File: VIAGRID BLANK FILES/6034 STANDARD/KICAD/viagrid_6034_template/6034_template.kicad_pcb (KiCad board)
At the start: 2 copper layers, 60 x 34 mm, 0 parts

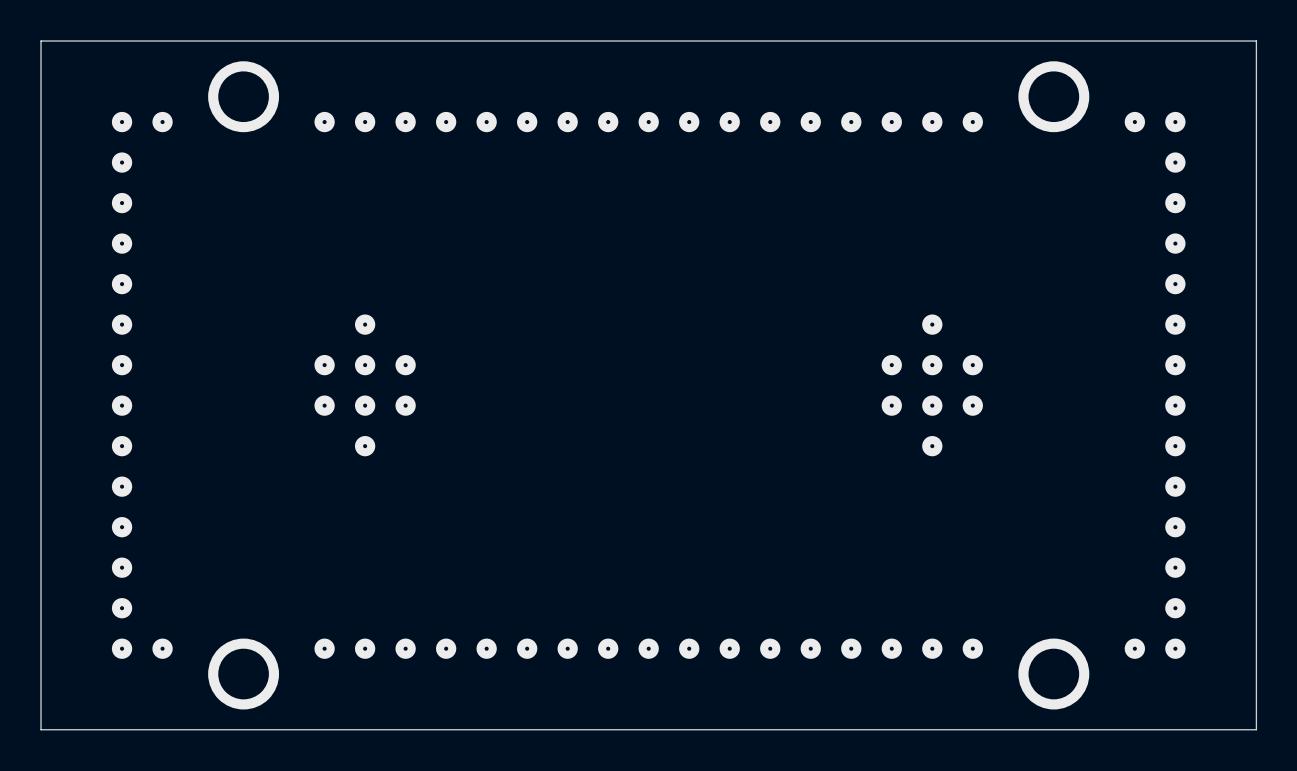
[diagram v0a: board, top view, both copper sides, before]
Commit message: added copper fill and soldermask
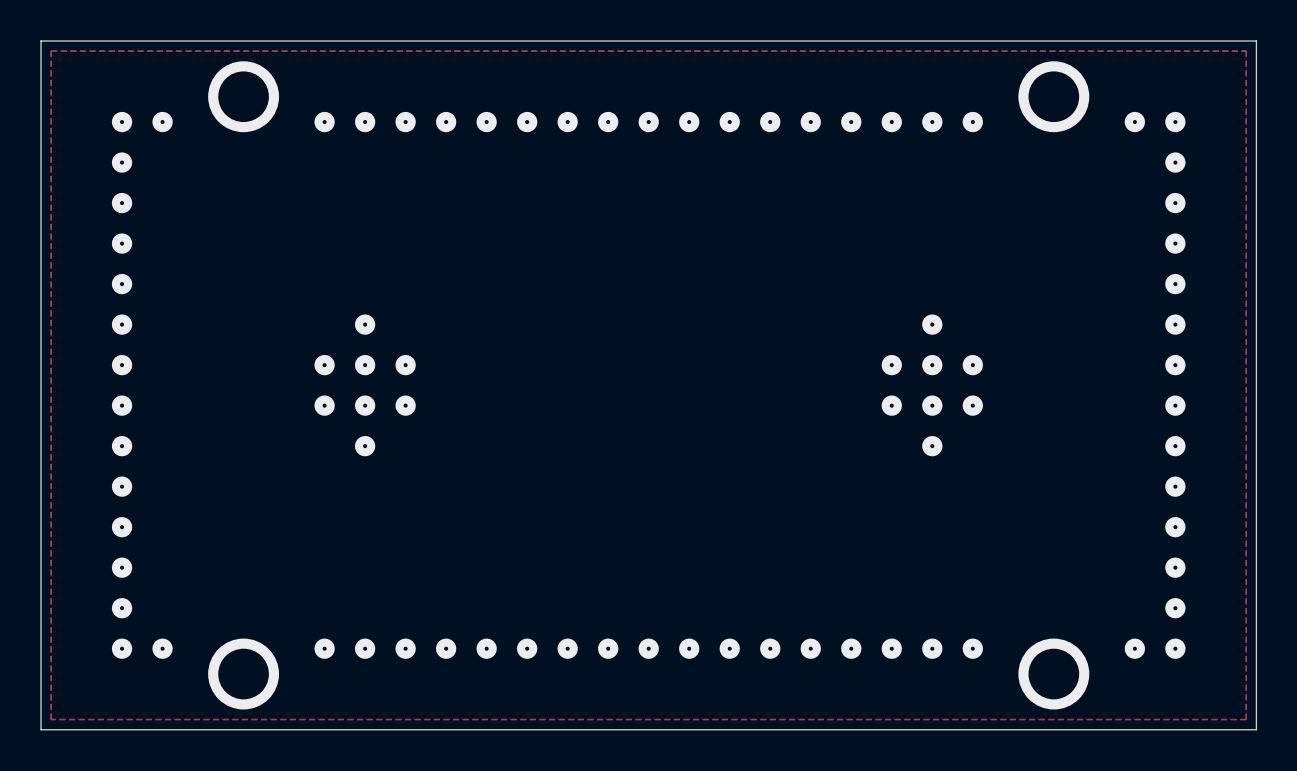
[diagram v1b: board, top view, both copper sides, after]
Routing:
- added copper zone on B.Cu, net GND
- added copper zone on F.Cu, net GND
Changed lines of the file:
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@@
 		(allow_soldermask_bridges_in_footprints no)
 		(tenting front back)
+		(aux_axis_origin 118.5011 122.0036)
+		(grid_origin 118.5011 122.0036)
 		(pcbplotparams
 			(layerselection 0x00000000_00000000_55555555_5755f5ff)
@@
 			(plotframeref no)
 			(mode 1)
-			(useauxorigin no)
+			(useauxorigin yes)
 			(hpglpennumber 1)
 			(hpglpenspeed 20)
@@
 			(outputformat 1)
 			(mirror no)
-			(drillshape 1)
+			(drillshape 0)
 			(scaleselection 1)
-			(outputdirectory "")
+			(outputdirectory "export/")
 		)
 	)
@@
 		(net 1)
 	)
+	(zone
+		(net 1)
+		(net_name "GND")
+		(layer "F.Cu")
+		(hatch edge 0.5)
+		(connect_pads
+			(clearance 0.5)
+		)
+		(min_thickness 0.25)
+		(filled_areas_thickness no)
+		(fill yes
+			(thermal_gap 0.5)
+			(thermal_bridge_width 0.5)
+		)
+		(polygon
+			(pts
+				(xy 119 88.5) (xy 178 88.5) (xy 178 121.5) (xy 119 121.5)
+			)
+		)
+	)
+	(zone
+		(net 1)
+		(net_name "GND")
+		(layer "B.Cu")
+		(hatch edge 0.5)
+		(connect_pads
+			(clearance 0.5)
+		)
+		(min_thickness 0.25)
+		(filled_areas_thickness no)
+		(fill yes
+			(thermal_gap 0.5)
+			(thermal_bridge_width 0.5)
+		)
+		(polygon
+			(pts
+				(xy 119 88.5) (xy 178 88.5) (xy 178 121.5) (xy 119 121.5)
+			)
+		)
+	)
 	(embedded_fonts no)
